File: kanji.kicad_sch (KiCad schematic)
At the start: 30 parts, among them J3 E-Ink, Q1 AO3400A, U3 SHT4x, U4 XIAO-ESP32-S3-SMD

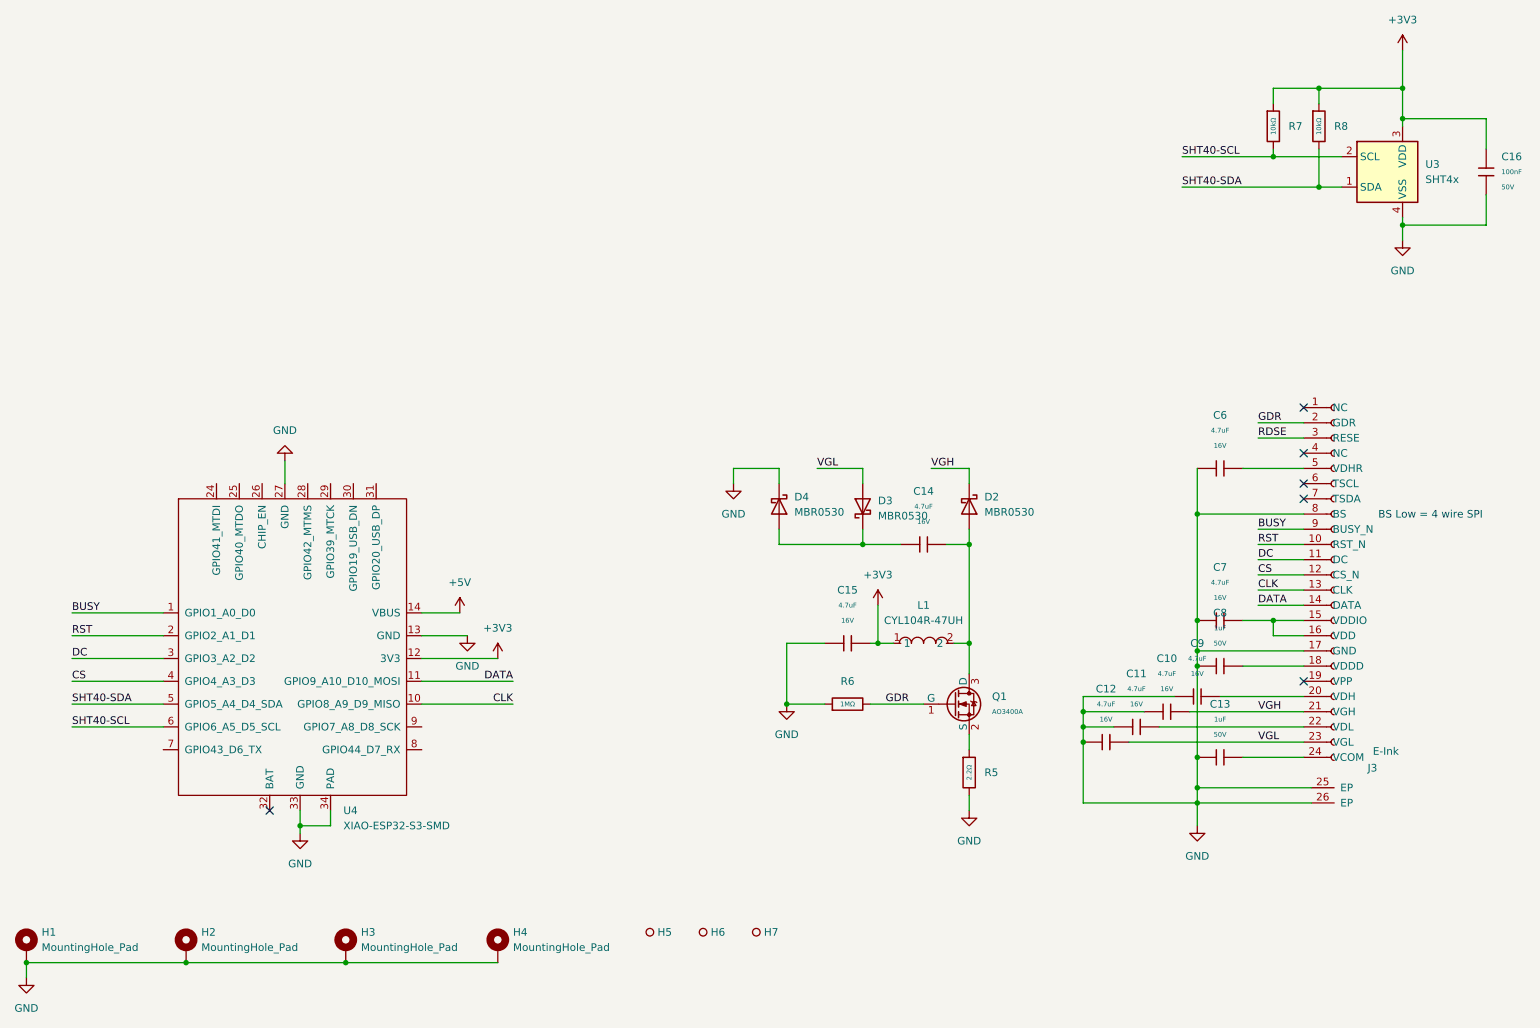
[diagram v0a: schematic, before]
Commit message: feat: add light sensor
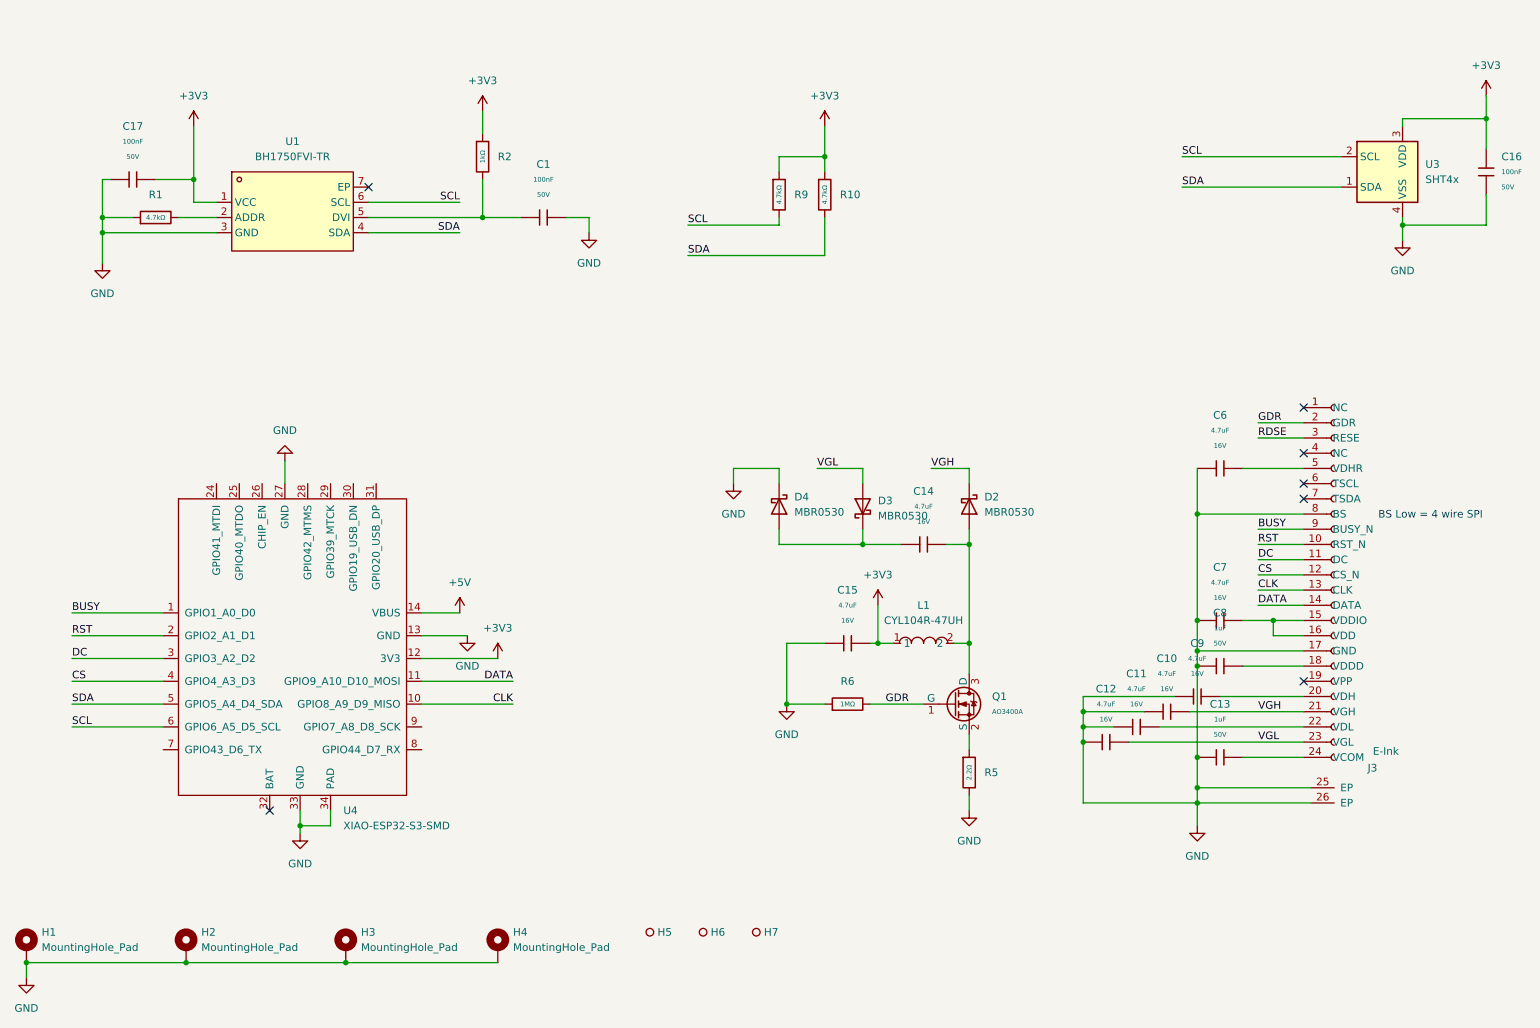
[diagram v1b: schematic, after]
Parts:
- removed R7, R8: 10kΩ, PCM_JLCPCB:R_0603, symbol PCM_JLCPCB-Resistors:0603,10kΩ
- added C1, C17: 100nF, PCM_JLCPCB:C_0603, symbol PCM_JLCPCB-Capacitors:0603,100nF
- added R1, R10, R9: 4.7kΩ, PCM_JLCPCB:R_0603, symbol PCM_JLCPCB-Resistors:0603,4.7kΩ
- added R2: 1kΩ, PCM_JLCPCB:R_0603, symbol PCM_JLCPCB-Resistors:0603,1kΩ
- added U1: BH1750FVI-TR, easyeda2kicad:WSOF-6_L2.6-W1.6-P0.50-TL-EP, symbol easyeda2kicad:BH1750FVI-TR
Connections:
- net +3V3: now also C17.2, R10.1, R2.1, R9.1, U1.1 (VCC)
- net GND: now also C1.2, C17.1, R1.1, U1.3 (GND)
- net SHT40-SCL renamed SCL
- net SCL: now also R9.2, U1.6 (SCL)
- net SHT40-SDA renamed SDA
- net SDA: now also R10.2, U1.4 (SDA)
- new net: R1.2, U1.2 (ADDR)
- new net: C1.1, R2.2, U1.5 (DVI)
- no-connect marks 6 -> 7
